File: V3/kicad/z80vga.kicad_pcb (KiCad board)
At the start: 2 copper layers, 135 x 100 mm, 59 parts, among them J1000 Barrel_Jack_Switch, J2120 USB_B, J2121 Conn_01x03_Male, J2122 Conn_01x02_Male, J2200 Conn_01x08_Male, J2201 Conn_01x08_Male, J2210 Micro_SD_Card_Det, J2220 AVR-ISP-6, J2221 Conn_01x02_Male, SW2110 SW_Push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

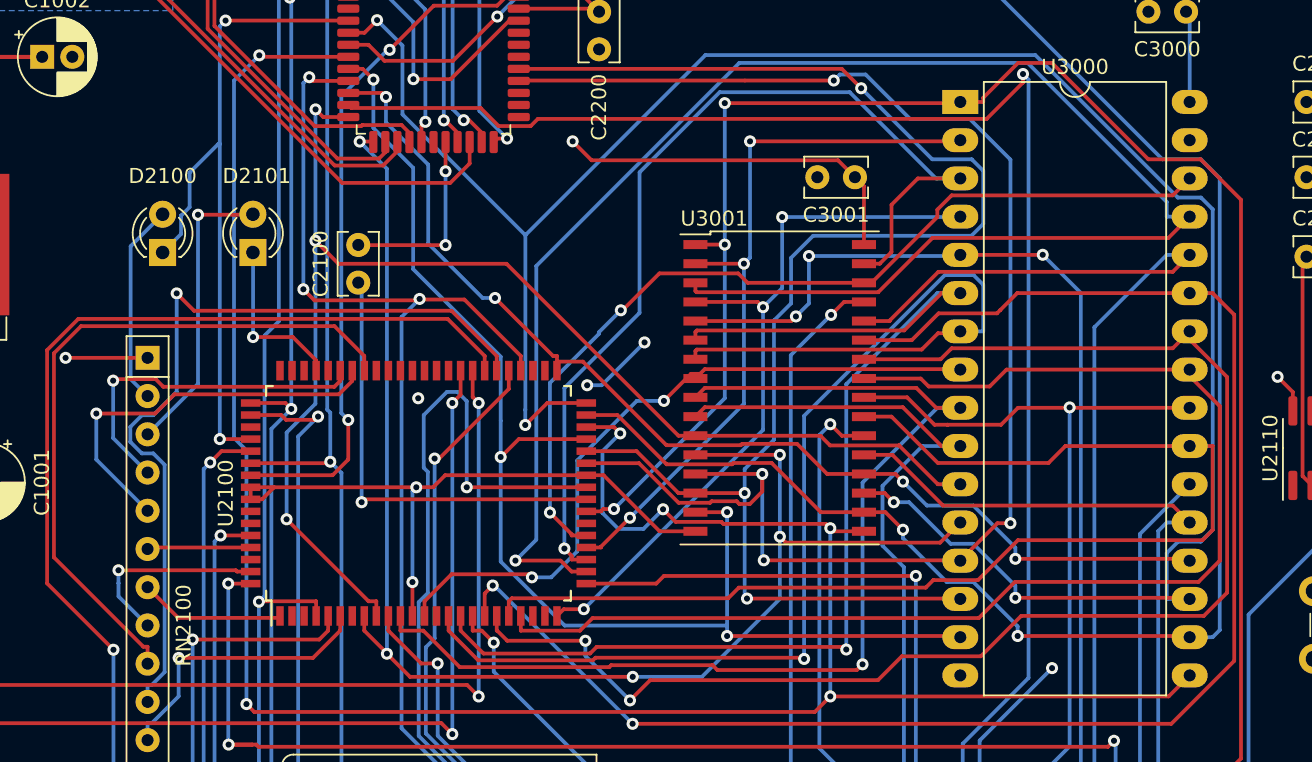
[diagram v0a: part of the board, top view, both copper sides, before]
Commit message: Reworking 3.0 board
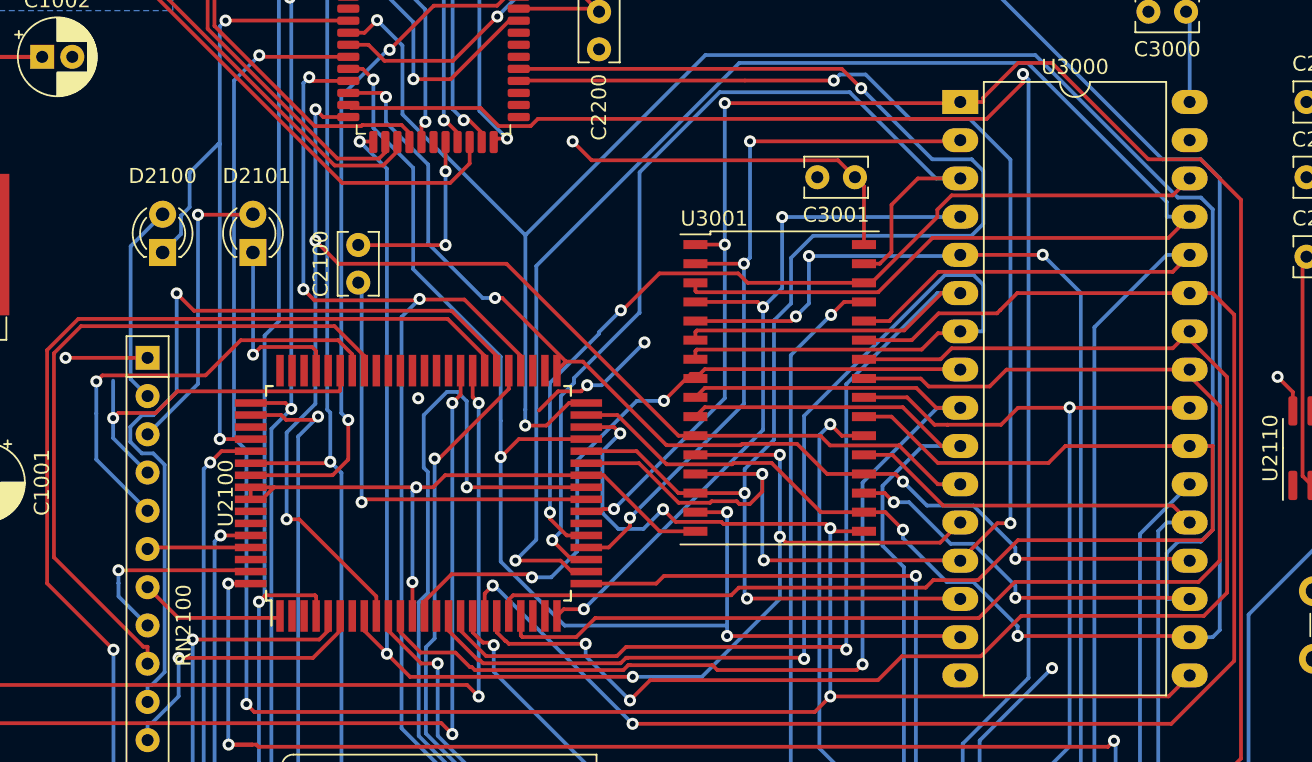
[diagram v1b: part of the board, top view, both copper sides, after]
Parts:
- removed REF**: KiCad-Logo2_5mm_SilkScreen, Symbol:KiCad-Logo2_5mm_SilkScreen
- U2100: footprint Package_QFP:PQFP-80_14x20mm_P0.8mm -> Z180-Custom-Footprint:PQFP-80_14x20mm_P0.8mm
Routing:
- net GND: track 110.5 -> 114.4 mm
- net /2000_Z80/2100_ALTCPU/CKS: track 26.5 -> 29.6 mm
- net /2000_Z80/2100_ALTCPU/HALT: track 11.1 -> 13.3 mm
- net /2000_Z80/2100_ALTCPU/DREQ1: track 23.2 -> 24.2 mm
- net /3000_Memory/A15: track 65.4 -> 66.1 mm
- net /2000_Z80/2100_ALTCPU/INT: track 89.7 -> 90.2 mm
- net /3000_Memory/A11: track 85.4 -> 85.9 mm

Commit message: cleared out old memory traces
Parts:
- moved C2112 28.0 mm to (157.0, 57.0), turned to 0 degrees
- moved U2110 6.40 mm to (156.0, 84.0)
- moved C3000 5.41 mm to (146.5, 56.0)
- moved C3001 5.41 mm to (124.5, 67.0)
- moved U3000 5.41 mm to (131.5, 62.0)
- moved U3001 5.41 mm to (119.5, 81.0)
- moved RN2110 5.22 mm to (159.5, 72.0)
- moved SW2110 4.92 mm to (159.0, 97.5)
- moved C2110 3.35 mm to (151.5, 62.0)
- moved C2111 3.35 mm to (151.5, 67.0)
- moved C2113 3.35 mm to (151.5, 72.3)
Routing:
- net /3000_Memory/D4: track 144.4 -> 20.3 mm, vias 3 -> 1
- net /3000_Memory/A18: track 129.3 -> 6.98 mm, vias 3 -> 1
- net /3000_Memory/D5: track 147.5 -> 38.0 mm, vias 4 -> 2
- net /3000_Memory/D0: track 101.4 -> 3.54 mm, vias 4 -> 0
- net /3000_Memory/D1: track 100.7 -> 3.34 mm, vias 3 -> 0
- net /3000_Memory/A13: track 126.0 -> 30.4 mm, vias 1 -> 0
- net /3000_Memory/A8: track 106.5 -> 15.3 mm
- net /3000_Memory/A14: track 114.5 -> 25.2 mm
- net /3000_Memory/D3: track 152.3 -> 64.0 mm, vias 6 -> 4
- net /2000_Z80/2200_PERP_ALT/CS: track 98.4 -> 13.4 mm, vias 1 -> 0
- net /3000_Memory/A9: track 95.6 -> 14.2 mm
- net /3000_Memory/A11: track 85.9 -> 6.81 mm
- net /3000_Memory/A10: track 80.3 -> 1.50 mm
- net /3000_Memory/A5: track 81.2 -> 14.0 mm, vias 1 -> 0
- net /3000_Memory/A15: track 66.1 -> 2.82 mm
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
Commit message: started on rerouting
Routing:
- net /2000_Z80/2100_ALTCPU/A19: track 90.7 -> 7.94 mm
- net /2000_Z80/2100_ALTCPU/RTS0: track 69.8 -> 8.06 mm
- net /2000_Z80/2100_ALTCPU/2110_Reset/Reset: track 10.1 -> 51.7 mm, vias 1 -> 2
- net /3000_Memory/D7: track 130.1 -> 88.9 mm, vias 3 -> 5
- net /3000_Memory/D5: track 38.0 -> 78.5 mm, vias 2 -> 4
- net Net-(C2113-Pad1): track 6.50 -> 44.5 mm
- net /3000_Memory/D3: track 64.0 -> 100.3 mm, vias 4 -> 6
- net /3000_Memory/D4: track 20.3 -> 52.8 mm, vias 1 -> 3
- net /3000_Memory/A12: track 1.97 -> 34.1 mm, vias 1 -> 3
- net /3000_Memory/A16: track 4.05 -> 34.3 mm, vias 1 -> 3
- net Net-(C2111-Pad1): track 0.00 -> 28.8 mm, vias 0 -> 1
- net /3000_Memory/A17: track 22.3 -> 49.3 mm, vias 2 -> 4
- net /3000_Memory/D2: track 49.7 -> 75.4 mm, vias 2 -> 4
- net Net-(C2112-Pad1): track 0.00 -> 25.0 mm, vias 0 -> 1
- net /3000_Memory/A15: track 2.82 -> 27.4 mm, vias 1 -> 3
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
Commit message: on to autoroute
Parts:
- U3001: footprint Package_SO:TSOP-II-32_21.0x10.2mm_P1.27mm -> Package_SO:SSOP-32_11.305x20.495mm_P1.27mm
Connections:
- U2101 pad 12: /2000_Z80/2100_ALTCPU/C_RST -> /2000_Z80/ROM_CS
- U2101 pad 19: /2000_Z80/ROM_CS -> /2000_Z80/2100_ALTCPU/C_RST
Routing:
- net /2000_Z80/WRITE: track 19.7 -> 69.5 mm, vias 1 -> 2
- net /2000_Z80/2100_ALTCPU/C_RST: track 12.2 -> 55.3 mm
- net /2000_Z80/READ: track 22.3 -> 58.5 mm
- net /2000_Z80/RAM_CS: track 0.00 -> 31.6 mm, vias 0 -> 1
- net /2000_Z80/ROM_CS: track 0.00 -> 28.9 mm
- net /3000_Memory/A16: track 34.3 -> 40.0 mm
- net /3000_Memory/A17: track 49.3 -> 52.0 mm
- net /3000_Memory/D0: track 27.6 -> 29.1 mm
- net /3000_Memory/A6: track 31.8 -> 32.8 mm
- net /3000_Memory/D7: track 88.9 -> 88.0 mm
- net /3000_Memory/A9: track 36.6 -> 35.7 mm
- net /3000_Memory/A8: track 38.3 -> 37.3 mm
- net /3000_Memory/A13: track 30.2 -> 29.2 mm
- net /3000_Memory/A1: track 58.8 -> 59.8 mm
- net /3000_Memory/A10: track 23.9 -> 23.0 mm
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
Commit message: little more cleanup
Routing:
- net /2000_Z80/2200_PERP_ALT/CS: track 13.4 -> 99.2 mm, vias 0 -> 1
- net /3000_Memory/A17: track 52.0 -> 73.5 mm
- net /3000_Memory/A3: track 35.5 -> 17.9 mm
- net /3000_Memory/A0: track 75.4 -> 58.4 mm, vias 3 -> 2
- net /3000_Memory/A5: track 32.3 -> 19.3 mm
- net /3000_Memory/A6: track 32.8 -> 20.8 mm
- net /3000_Memory/A2: track 24.5 -> 19.4 mm, vias 1 -> 0
- net GND: track 96.9 -> 91.9 mm, vias 9 -> 8
- net /3000_Memory/D4: track 52.8 -> 50.7 mm
- net /3000_Memory/A9: track 35.7 -> 33.8 mm

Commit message: more cleanup
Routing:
- net /2000_Z80/2100_ALTCPU/A19: track 7.94 -> 88.8 mm, vias 1 -> 2
- net /2000_Z80/2100_ALTCPU/RTS0: track 8.06 -> 76.4 mm, vias 1 -> 2
- net /3000_Memory/D1: track 24.3 -> 85.8 mm, vias 2 -> 3
- net /3000_Memory/A0: track 58.4 -> 114.5 mm, vias 2 -> 3
- net /3000_Memory/D0: track 29.1 -> 79.0 mm, vias 2 -> 3
- net /3000_Memory/D4: track 50.7 -> 84.5 mm, vias 3 -> 4
- net /3000_Memory/A4: track 44.5 -> 18.4 mm, vias 2 -> 0
- net /3000_Memory/A8: track 37.3 -> 22.0 mm, vias 2 -> 0
- net /3000_Memory/A9: track 33.8 -> 21.5 mm, vias 2 -> 0
- net +5V: track 172.0 -> 161.8 mm, vias 8 -> 7
- net /3000_Memory/D3: track 100.3 -> 91.4 mm
- net /3000_Memory/A7: track 68.4 -> 76.3 mm
- net /2000_Z80/WRITE: track 69.5 -> 62.3 mm
- net /3000_Memory/A14: track 43.2 -> 36.2 mm, vias 3 -> 2
- net /3000_Memory/A17: track 73.5 -> 80.3 mm
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
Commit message: ill let the autoroute do the rest
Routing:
- net /3000_Memory/A18: track 27.0 -> 122.9 mm, vias 2 -> 5
- net /3000_Memory/D6: track 49.1 -> 85.7 mm, vias 4 -> 6
- net /3000_Memory/D4: track 84.5 -> 115.5 mm, vias 4 -> 5
- net /3000_Memory/D7: track 88.0 -> 118.6 mm
- net /3000_Memory/D3: track 91.4 -> 115.4 mm
- net /3000_Memory/D5: track 78.5 -> 97.8 mm
- net GND: track 89.2 -> 91.6 mm, vias 7 -> 9
- net /3000_Memory/A0: track 114.5 -> 115.0 mm

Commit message: reroute complete
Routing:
- net /3000_Memory/A2: track 19.4 -> 127.7 mm, vias 0 -> 2
- net /3000_Memory/A5: track 19.3 -> 121.3 mm
- net /3000_Memory/A8: track 22.0 -> 106.4 mm, vias 0 -> 2
- net /3000_Memory/A11: track 21.7 -> 96.4 mm
- net /3000_Memory/A10: track 21.5 -> 93.7 mm, vias 0 -> 1
- net /3000_Memory/A1: track 59.9 -> 121.9 mm, vias 3 -> 4
- net /3000_Memory/A7: track 76.3 -> 132.6 mm
- net GND: track 91.6 -> 147.9 mm, vias 9 -> 11
- net +5V: track 161.8 -> 217.5 mm, vias 7 -> 11
- net /3000_Memory/A9: track 21.5 -> 68.4 mm, vias 0 -> 2
- net /3000_Memory/A13: track 23.9 -> 70.0 mm, vias 2 -> 4
- net /3000_Memory/A15: track 24.6 -> 68.0 mm, vias 2 -> 3
- net /3000_Memory/A6: track 20.8 -> 63.1 mm, vias 0 -> 2
- net /3000_Memory/A3: track 17.9 -> 55.7 mm, vias 0 -> 2
- net /3000_Memory/A4: track 18.4 -> 54.8 mm, vias 0 -> 2
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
